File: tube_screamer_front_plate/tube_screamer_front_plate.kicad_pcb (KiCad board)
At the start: 2 copper layers, 80 x 100 mm, 12 parts, among them J1 top_panel_connector

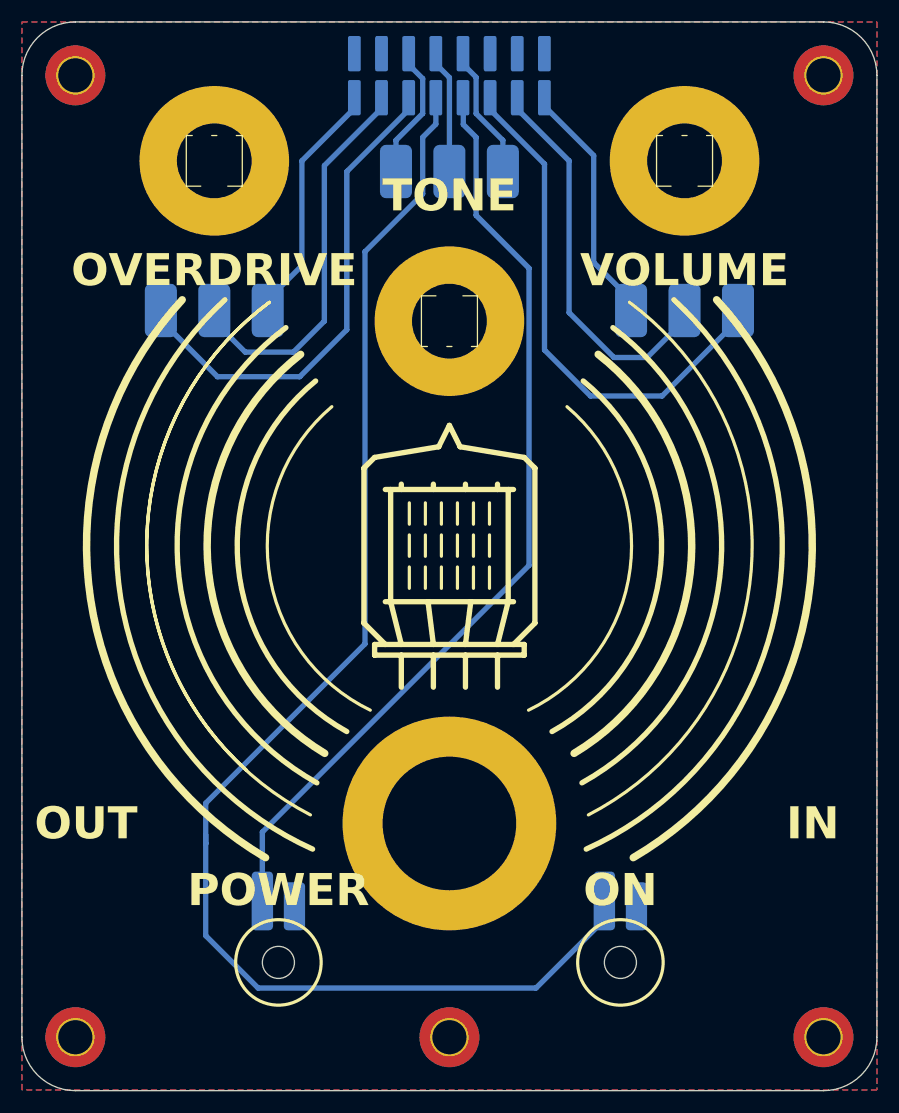
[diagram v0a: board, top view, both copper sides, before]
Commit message: Top plate rounded.
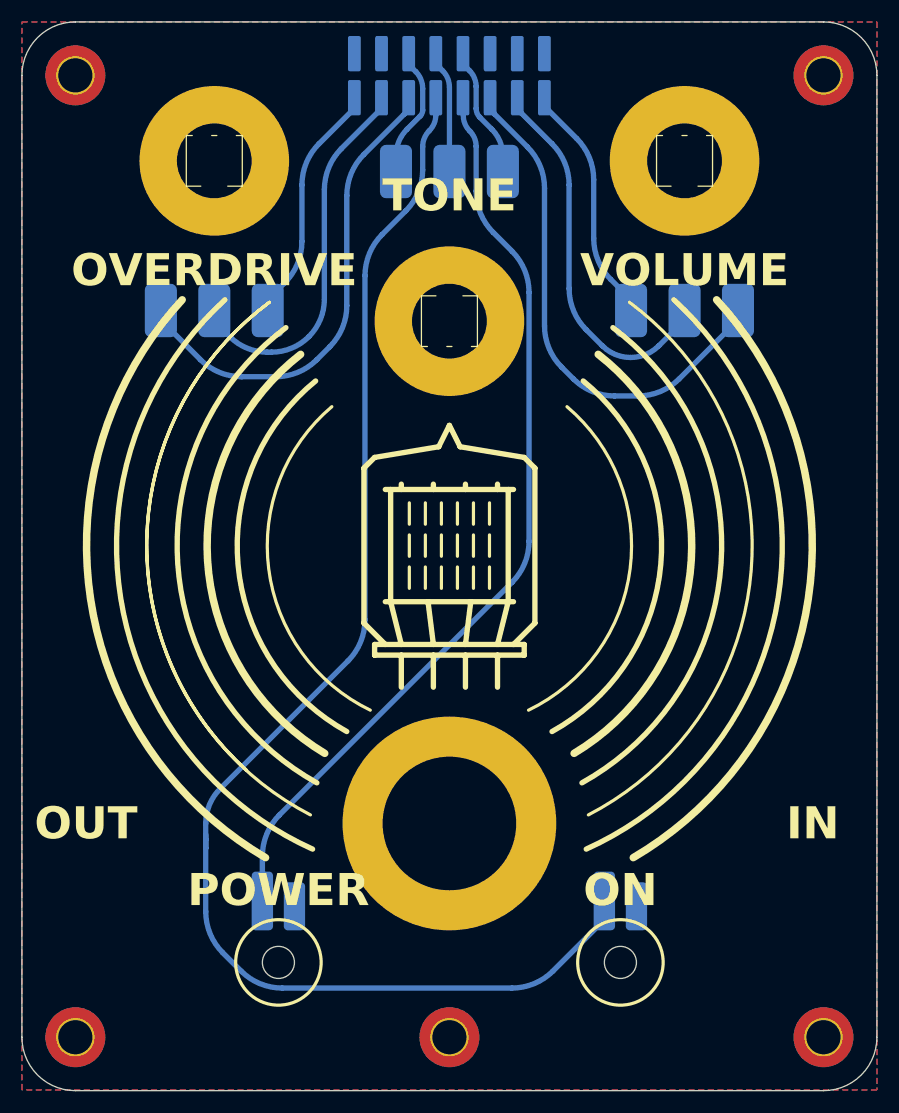
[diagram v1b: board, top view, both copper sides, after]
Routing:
- net Net-(D1-A): track 131.9 -> 130.2 mm
- net Net-(D2-A): track 88.1 -> 86.8 mm
- net Net-(J1A-Pin_6): track 46.4 -> 45.3 mm
- net Net-(J1C-Pin_12): track 48.0 -> 46.9 mm
- net Net-(J1A-Pin_4): track 36.8 -> 35.7 mm
- net Net-(J1C-Pin_14): track 37.0 -> 36.0 mm
- net Net-(J1A-Pin_2): track 23.3 -> 22.6 mm
- net Net-(J1C-Pin_16): track 23.3 -> 22.6 mm
